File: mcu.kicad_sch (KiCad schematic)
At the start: 17 parts

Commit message: Annotate schematic
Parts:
- gave numbers to parts that had none: 17
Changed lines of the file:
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@@
   (symbol (lib_id "power:+3V3") (at 74.93 38.1 0) (unit 1)
     (in_bom yes) (on_board yes) (fields_autoplaced)
-    (property "Reference" "#PWR0117" (id 0) (at 74.93 41.91 0)
+    (property "Reference" "#PWR0303" (id 0) (at 74.93 41.91 0)
       (effects (font (size 1.27 1.27)) hide)
     )
@@
   (symbol (lib_id "power:+3V3") (at 195.58 29.21 0) (unit 1)
     (in_bom yes) (on_board yes) (fields_autoplaced)
-    (property "Reference" "#PWR?" (id 0) (at 195.58 33.02 0)
+    (property "Reference" "#PWR0307" (id 0) (at 195.58 33.02 0)
       (effects (font (size 1.27 1.27)) hide)
     )
@@
   (symbol (lib_id "power:+3V3") (at 228.6 52.07 0) (unit 1)
     (in_bom yes) (on_board yes) (fields_autoplaced)
-    (property "Reference" "#PWR?" (id 0) (at 228.6 55.88 0)
+    (property "Reference" "#PWR0309" (id 0) (at 228.6 55.88 0)
       (effects (font (size 1.27 1.27)) hide)
     )
@@
   (symbol (lib_id "power:GND") (at 49.53 60.96 0) (unit 1)
     (in_bom yes) (on_board yes) (fields_autoplaced)
-    (property "Reference" "#PWR0118" (id 0) (at 49.53 67.31 0)
+    (property "Reference" "#PWR0301" (id 0) (at 49.53 67.31 0)
       (effects (font (size 1.27 1.27)) hide)
     )
@@
   (symbol (lib_id "power:GND") (at 64.77 58.42 0) (unit 1)
     (in_bom yes) (on_board yes) (fields_autoplaced)
-    (property "Reference" "#PWR0116" (id 0) (at 64.77 64.77 0)
+    (property "Reference" "#PWR0302" (id 0) (at 64.77 64.77 0)
       (effects (font (size 1.27 1.27)) hide)
     )
@@
   (symbol (lib_id "power:GND") (at 139.7 140.97 0) (unit 1)
     (in_bom yes) (on_board yes) (fields_autoplaced)
-    (property "Reference" "#PWR0119" (id 0) (at 139.7 147.32 0)
+    (property "Reference" "#PWR0304" (id 0) (at 139.7 147.32 0)
       (effects (font (size 1.27 1.27)) hide)
     )
@@
   (symbol (lib_id "power:GND") (at 142.24 58.42 0) (unit 1)
     (in_bom yes) (on_board yes) (fields_autoplaced)
-    (property "Reference" "#PWR0122" (id 0) (at 142.24 64.77 0)
+    (property "Reference" "#PWR0305" (id 0) (at 142.24 64.77 0)
       (effects (font (size 1.27 1.27)) hide)
     )
@@
   (symbol (lib_id "power:GND") (at 176.53 97.79 0) (unit 1)
     (in_bom yes) (on_board yes) (fields_autoplaced)
-    (property "Reference" "#PWR?" (id 0) (at 176.53 104.14 0)
+    (property "Reference" "#PWR0306" (id 0) (at 176.53 104.14 0)
       (effects (font (size 1.27 1.27)) hide)
     )
@@
   (symbol (lib_id "power:GND") (at 196.85 58.42 0) (unit 1)
     (in_bom yes) (on_board yes) (fields_autoplaced)
-    (property "Reference" "#PWR?" (id 0) (at 196.85 64.77 0)
+    (property "Reference" "#PWR0308" (id 0) (at 196.85 64.77 0)
       (effects (font (size 1.27 1.27)) hide)
     )
@@
   (symbol (lib_id "power:GND") (at 243.84 49.53 0) (unit 1)
     (in_bom yes) (on_board yes) (fields_autoplaced)
-    (property "Reference" "#PWR?" (id 0) (at 243.84 55.88 0)
+    (property "Reference" "#PWR0310" (id 0) (at 243.84 55.88 0)
       (effects (font (size 1.27 1.27)) hide)
     )
@@
   (symbol (lib_id "Device:R") (at 74.93 44.45 0) (unit 1)
     (in_bom yes) (on_board yes)
-    (property "Reference" "R?" (id 0) (at 77.47 43.1799 0)
+    (property "Reference" "R301" (id 0) (at 77.47 43.1799 0)
       (effects (font (size 1.27 1.27)) (justify left))
     )
@@
   (symbol (lib_id "Device:R") (at 135.89 55.88 90) (unit 1)
     (in_bom yes) (on_board yes)
-    (property "Reference" "R?" (id 0) (at 135.89 53.34 90))
+    (property "Reference" "R302" (id 0) (at 135.89 53.34 90))
     (property "Value" "10K" (id 1) (at 135.89 55.88 90))
     (property "Footprint" "" (id 2) (at 135.89 57.658 90)
@@
   (symbol (lib_id "Device:R") (at 148.59 95.25 90) (unit 1)
     (in_bom yes) (on_board yes)
-    (property "Reference" "R?" (id 0) (at 148.59 92.71 90))
+    (property "Reference" "R303" (id 0) (at 148.59 92.71 90))
     (property "Value" "22R" (id 1) (at 148.59 95.25 90))
     (property "Footprint" "" (id 2) (at 148.59 97.028 90)
@@
   (symbol (lib_id "Device:R") (at 148.59 97.79 90) (unit 1)
     (in_bom yes) (on_board yes)
-    (property "Reference" "R?" (id 0) (at 148.59 100.33 90))
+    (property "Reference" "R304" (id 0) (at 148.59 100.33 90))
     (property "Value" "22R" (id 1) (at 148.59 97.79 90))
     (property "Footprint" "" (id 2) (at 148.59 99.568 90)
@@
   (symbol (lib_id "Device:R") (at 153.67 104.14 0) (unit 1)
     (in_bom yes) (on_board yes)
-    (property "Reference" "R?" (id 0) (at 156.21 102.8699 0)
+    (property "Reference" "R305" (id 0) (at 156.21 102.8699 0)
       (effects (font (size 1.27 1.27)) (justify left))
     )
@@
   (symbol (lib_id "Device:R") (at 176.53 93.98 0) (unit 1)
     (in_bom yes) (on_board yes)
-    (property "Reference" "R?" (id 0) (at 171.45 92.7099 0)
+    (property "Reference" "R306" (id 0) (at 170.18 92.7099 0)
       (effects (font (size 1.27 1.27)) (justify left))
     )
@@
   (symbol (lib_id "Device:R") (at 180.34 90.17 90) (unit 1)
     (in_bom yes) (on_board yes)
-    (property "Reference" "R?" (id 0) (at 180.34 87.63 90))
+    (property "Reference" "R307" (id 0) (at 180.34 87.63 90))
     (property "Value" "4.7k" (id 1) (at 180.34 90.17 90))
     (property "Footprint" "" (id 2) (at 180.34 91.948 90)
@@
   (symbol (lib_id "Device:R") (at 191.77 35.56 0) (unit 1)
     (in_bom yes) (on_board yes)
-    (property "Reference" "R?" (id 0) (at 186.69 34.2899 0)
+    (property "Reference" "R308" (id 0) (at 184.15 34.2899 0)
       (effects (font (size 1.27 1.27)) (justify left))
     )
@@
   (symbol (lib_id "Device:R") (at 243.84 45.72 0) (unit 1)
     (in_bom yes) (on_board yes)
-    (property "Reference" "R?" (id 0) (at 238.76 44.4499 0)
-      (effects (font (size 1.27 1.27)) (justify left))
-    )
-    (property "Value" "64K" (id 1) (at 237.49 46.9899 0)
+    (property "Reference" "R309" (id 0) (at 245.11 44.4499 0)
+      (effects (font (size 1.27 1.27)) (justify left))
+    )
+    (property "Value" "64K" (id 1) (at 245.11 46.9899 0)
       (effects (font (size 1.27 1.27)) (justify left))
     )
@@
   (symbol (lib_id "Device:C") (at 64.77 54.61 0) (unit 1)
     (in_bom yes) (on_board yes)
-    (property "Reference" "C?" (id 0) (at 68.58 53.3399 0)
+    (property "Reference" "C301" (id 0) (at 68.58 53.3399 0)
       (effects (font (size 1.27 1.27)) (justify left))
     )
@@
   (symbol (lib_id "Device:C") (at 134.62 133.35 0) (unit 1)
     (in_bom yes) (on_board yes)
-    (property "Reference" "C?" (id 0) (at 135.89 130.8099 0)
+    (property "Reference" "C302" (id 0) (at 135.89 130.8099 0)
       (effects (font (size 1.27 1.27)) (justify left))
     )
@@
   (symbol (lib_id "Device:C") (at 144.78 133.35 0) (unit 1)
     (in_bom yes) (on_board yes)
-    (property "Reference" "C?" (id 0) (at 145.415 130.81 0)
+    (property "Reference" "C303" (id 0) (at 145.415 130.81 0)
       (effects (font (size 1.27 1.27)) (justify left))
     )
@@
   (symbol (lib_id "Device:C") (at 209.55 54.61 270) (unit 1)
     (in_bom yes) (on_board yes)
-    (property "Reference" "C?" (id 0) (at 209.55 60.96 90))
+    (property "Reference" "C304" (id 0) (at 209.55 60.96 90))
     (property "Value" "100nF" (id 1) (at 209.55 58.42 90))
     (property "Footprint" "" (id 2) (at 205.74 55.5752 0)
@@
   (symbol (lib_id "Switch:SW_Push") (at 49.53 55.88 90) (unit 1)
     (in_bom yes) (on_board yes) (fields_autoplaced)
-    (property "Reference" "SW?" (id 0) (at 50.8 54.6099 90)
+    (property "Reference" "SW301" (id 0) (at 50.8 54.6099 90)
       (effects (font (size 1.27 1.27)) (justify right))
     )
@@
   (symbol (lib_id "Device:Crystal") (at 139.7 124.46 0) (unit 1)
     (in_bom yes) (on_board yes) (fields_autoplaced)
-    (property "Reference" "Y?" (id 0) (at 139.7 116.84 0))
+    (property "Reference" "Y301" (id 0) (at 139.7 116.84 0))
     (property "Value" "8MHz" (id 1) (at 139.7 119.38 0))
     (property "Footprint" "" (id 2) (at 139.7 124.46 0)
@@
   (symbol (lib_id "GozLib:M95640-WMN6TP") (at 209.55 38.1 0) (unit 1)
     (in_bom yes) (on_board yes) (fields_autoplaced)
-    (property "Reference" "U?" (id 0) (at 209.55 27.94 0))
+    (property "Reference" "U302" (id 0) (at 209.55 27.94 0))
     (property "Value" "M95640-WMN6TP" (id 1) (at 209.55 30.48 0))
     (property "Footprint" "Package_SO:SOIC-8_3.9x4.9mm_P1.27mm" (id 2) (at 207.01 19.05 0)
@@
   (symbol (lib_id "GozLib:STM32F103C8Tx") (at 104.14 68.58 0) (unit 1)
     (in_bom yes) (on_board yes) (fields_autoplaced)
-    (property "Reference" "U?" (id 0) (at 104.14 53.34 0))
+    (property "Reference" "U301" (id 0) (at 104.14 53.34 0))
     (property "Value" "STM32F103C8Tx" (id 1) (at 104.14 55.88 0))
     (property "Footprint" "Package_QFP:LQFP-48_7x7mm_P0.5mm" (id 2) (at 91.44 64.77 0)

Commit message: Clean up BOM
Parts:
- R301, R302: value 10K -> 10k
- R308, R309: value 64K -> 62k
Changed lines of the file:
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@@
       (effects (font (size 1.27 1.27)) (justify left))
     )
-    (property "Value" "10K" (id 1) (at 77.47 45.7199 0)
+    (property "Value" "10k" (id 1) (at 77.47 45.7199 0)
       (effects (font (size 1.27 1.27)) (justify left))
     )
@@
     (in_bom yes) (on_board yes)
     (property "Reference" "R302" (id 0) (at 135.89 53.34 90))
-    (property "Value" "10K" (id 1) (at 135.89 55.88 90))
+    (property "Value" "10k" (id 1) (at 135.89 55.88 90))
     (property "Footprint" "" (id 2) (at 135.89 57.658 90)
       (effects (font (size 1.27 1.27)) hide)
@@
       (effects (font (size 1.27 1.27)) (justify left))
     )
-    (property "Value" "64K" (id 1) (at 185.42 36.8299 0)
+    (property "Value" "62k" (id 1) (at 185.42 36.8299 0)
       (effects (font (size 1.27 1.27)) (justify left))
     )
@@
       (effects (font (size 1.27 1.27)) (justify left))
     )
-    (property "Value" "64K" (id 1) (at 245.11 46.9899 0)
+    (property "Value" "62k" (id 1) (at 245.11 46.9899 0)
       (effects (font (size 1.27 1.27)) (justify left))
     )

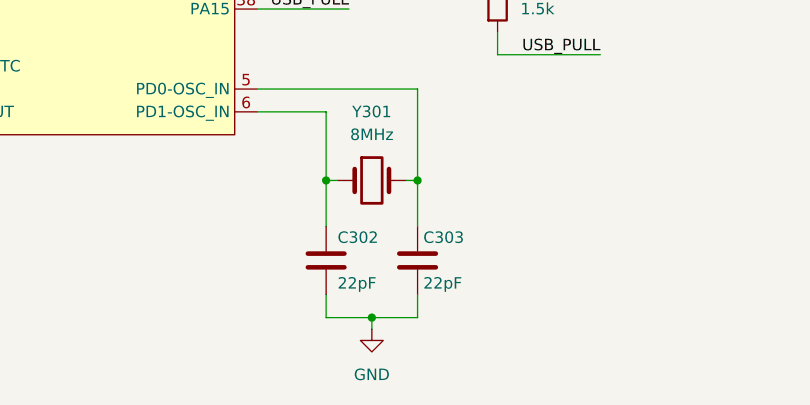
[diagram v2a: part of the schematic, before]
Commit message: Assign footprints
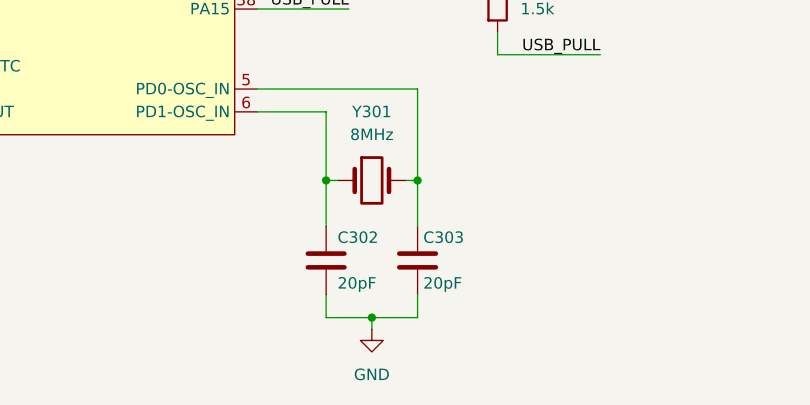
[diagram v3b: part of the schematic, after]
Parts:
- C301, C304: footprint (none) -> Capacitor_SMD:C_0805_2012Metric_Pad1.18x1.45mm_HandSolder
- C302, C303: value 22pF -> 20pF; footprint (none) -> Capacitor_SMD:C_0805_2012Metric_Pad1.18x1.45mm_HandSolder
- R301, R302, R303, R304, R305, R306, R307, R308, R309: footprint (none) -> Resistor_SMD:R_0805_2012Metric_Pad1.20x1.40mm_HandSolder
- SW301: footprint (none) -> Button_Switch_SMD:SW_SPST_TL3342
- Y301: footprint (none) -> Crystal:Crystal_SMD_HC49-SD_HandSoldering
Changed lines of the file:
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@@
       (effects (font (size 1.27 1.27)) (justify left))
     )
-    (property "Footprint" "" (id 2) (at 73.152 44.45 90)
+    (property "Footprint" "Resistor_SMD:R_0805_2012Metric_Pad1.20x1.40mm_HandSolder" (id 2) (at 73.152 44.45 90)
       (effects (font (size 1.27 1.27)) hide)
     )
@@
     (property "Reference" "R302" (id 0) (at 135.89 53.34 90))
     (property "Value" "10k" (id 1) (at 135.89 55.88 90))
-    (property "Footprint" "" (id 2) (at 135.89 57.658 90)
+    (property "Footprint" "Resistor_SMD:R_0805_2012Metric_Pad1.20x1.40mm_HandSolder" (id 2) (at 135.89 57.658 90)
       (effects (font (size 1.27 1.27)) hide)
     )
@@
     (property "Reference" "R303" (id 0) (at 148.59 92.71 90))
     (property "Value" "22R" (id 1) (at 148.59 95.25 90))
-    (property "Footprint" "" (id 2) (at 148.59 97.028 90)
+    (property "Footprint" "Resistor_SMD:R_0805_2012Metric_Pad1.20x1.40mm_HandSolder" (id 2) (at 148.59 97.028 90)
       (effects (font (size 1.27 1.27)) hide)
     )
@@
     (property "Reference" "R304" (id 0) (at 148.59 100.33 90))
     (property "Value" "22R" (id 1) (at 148.59 97.79 90))
-    (property "Footprint" "" (id 2) (at 148.59 99.568 90)
+    (property "Footprint" "Resistor_SMD:R_0805_2012Metric_Pad1.20x1.40mm_HandSolder" (id 2) (at 148.59 99.568 90)
       (effects (font (size 1.27 1.27)) hide)
     )
@@
       (effects (font (size 1.27 1.27)) (justify left))
     )
-    (property "Footprint" "" (id 2) (at 151.892 104.14 90)
+    (property "Footprint" "Resistor_SMD:R_0805_2012Metric_Pad1.20x1.40mm_HandSolder" (id 2) (at 151.892 104.14 90)
       (effects (font (size 1.27 1.27)) hide)
     )
@@
       (effects (font (size 1.27 1.27)) (justify left))
     )
-    (property "Footprint" "" (id 2) (at 174.752 93.98 90)
+    (property "Footprint" "Resistor_SMD:R_0805_2012Metric_Pad1.20x1.40mm_HandSolder" (id 2) (at 174.752 93.98 90)
       (effects (font (size 1.27 1.27)) hide)
     )
@@
     (property "Reference" "R307" (id 0) (at 180.34 87.63 90))
     (property "Value" "4.7k" (id 1) (at 180.34 90.17 90))
-    (property "Footprint" "" (id 2) (at 180.34 91.948 90)
+    (property "Footprint" "Resistor_SMD:R_0805_2012Metric_Pad1.20x1.40mm_HandSolder" (id 2) (at 180.34 91.948 90)
       (effects (font (size 1.27 1.27)) hide)
     )
@@
       (effects (font (size 1.27 1.27)) (justify left))
     )
-    (property "Footprint" "" (id 2) (at 189.992 35.56 90)
+    (property "Footprint" "Resistor_SMD:R_0805_2012Metric_Pad1.20x1.40mm_HandSolder" (id 2) (at 189.992 35.56 90)
       (effects (font (size 1.27 1.27)) hide)
     )
@@
       (effects (font (size 1.27 1.27)) (justify left))
     )
-    (property "Footprint" "" (id 2) (at 242.062 45.72 90)
+    (property "Footprint" "Resistor_SMD:R_0805_2012Metric_Pad1.20x1.40mm_HandSolder" (id 2) (at 242.062 45.72 90)
       (effects (font (size 1.27 1.27)) hide)
     )
@@
       (effects (font (size 1.27 1.27)) (justify left))
     )
-    (property "Footprint" "" (id 2) (at 65.7352 58.42 0)
+    (property "Footprint" "Capacitor_SMD:C_0805_2012Metric_Pad1.18x1.45mm_HandSolder" (id 2) (at 65.7352 58.42 0)
       (effects (font (size 1.27 1.27)) hide)
     )
@@
       (effects (font (size 1.27 1.27)) (justify left))
     )
-    (property "Value" "22pF" (id 1) (at 135.89 135.8899 0)
-      (effects (font (size 1.27 1.27)) (justify left))
-    )
-    (property "Footprint" "" (id 2) (at 135.5852 137.16 0)
+    (property "Value" "20pF" (id 1) (at 135.89 135.8899 0)
+      (effects (font (size 1.27 1.27)) (justify left))
+    )
+    (property "Footprint" "Capacitor_SMD:C_0805_2012Metric_Pad1.18x1.45mm_HandSolder" (id 2) (at 135.5852 137.16 0)
       (effects (font (size 1.27 1.27)) hide)
     )
@@
       (effects (font (size 1.27 1.27)) (justify left))
     )
-    (property "Value" "22pF" (id 1) (at 145.415 135.89 0)
-      (effects (font (size 1.27 1.27)) (justify left))
-    )
-    (property "Footprint" "" (id 2) (at 145.7452 137.16 0)
+    (property "Value" "20pF" (id 1) (at 145.415 135.89 0)
+      (effects (font (size 1.27 1.27)) (justify left))
+    )
+    (property "Footprint" "Capacitor_SMD:C_0805_2012Metric_Pad1.18x1.45mm_HandSolder" (id 2) (at 145.7452 137.16 0)
       (effects (font (size 1.27 1.27)) hide)
     )
@@
     (property "Reference" "C304" (id 0) (at 209.55 60.96 90))
     (property "Value" "100nF" (id 1) (at 209.55 58.42 90))
-    (property "Footprint" "" (id 2) (at 205.74 55.5752 0)
+    (property "Footprint" "Capacitor_SMD:C_0805_2012Metric_Pad1.18x1.45mm_HandSolder" (id 2) (at 205.74 55.5752 0)
       (effects (font (size 1.27 1.27)) hide)
     )
@@
       (effects (font (size 1.27 1.27)) (justify right))
     )
-    (property "Footprint" "" (id 2) (at 44.45 55.88 0)
+    (property "Footprint" "Button_Switch_SMD:SW_SPST_TL3342" (id 2) (at 44.45 55.88 0)
       (effects (font (size 1.27 1.27)) hide)
     )
@@
     (property "Reference" "Y301" (id 0) (at 139.7 116.84 0))
     (property "Value" "8MHz" (id 1) (at 139.7 119.38 0))
-    (property "Footprint" "" (id 2) (at 139.7 124.46 0)
-      (effects (font (size 1.27 1.27)) hide)
-    )
+    (property "Footprint" "Crystal:Crystal_SMD_HC49-SD_HandSoldering" (id 2) (at 139.7 124.46 0)
+      (effects (font (size 1.27 1.27)) hide)
+    )
